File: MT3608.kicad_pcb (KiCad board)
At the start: 2 copper layers, 40 x 20 mm, 19 parts, among them J1 IN, J2 OUT, U1 MT3608

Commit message: Take 2
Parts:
- removed D1: SBR3U, Diode_SMD:D_PowerDI-123
- D2: value 1N4148 -> MBR0540; footprint Diode_THT:D_DO-35_SOD27_P7.62mm_Horizontal -> Diode_SMD:D_SOD-123
- moved TP6 13.7 mm to (102.8, 103.7)
- moved D2 12.5 mm to (113.1, 115.3), turned to 0 degrees
- moved TP2 11.4 mm to (107.9, 108.7)
- moved TP1 7.62 mm to (107.9, 103.7)
- moved R2 6.70 mm to (107.6, 118.0), turned to 180 degrees
- moved C4 5.50 mm to (107.7, 114.5), turned to 180 degrees
- moved R6 5.34 mm to (107.7, 112.0)
- moved J2 5.08 mm to (102.8, 108.7)
- moved TP7 5.08 mm to (102.8, 116.3)
- moved R1 1.16 mm to (112.8, 118.1), turned to 180 degrees
- moved L1 0.39 mm to (117.9, 106.6)
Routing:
- net Net-(D2-K): track 38.5 -> 12.9 mm, vias 1 -> 0
- net Net-(D2-A): track 30.2 -> 20.2 mm
- net Net-(U1-FB): track 11.4 -> 21.4 mm, vias 0 -> 2
- net Net-(J2-Pin_1): track 10.8 -> 5.25 mm
- net GND: track 0.00 -> 5.01 mm
- net Net-(U1-EN): track 23.1 -> 25.3 mm
- added copper zone on B.Cu, net GND
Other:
- board size 40 x 20 mm -> 35 x 22 mm

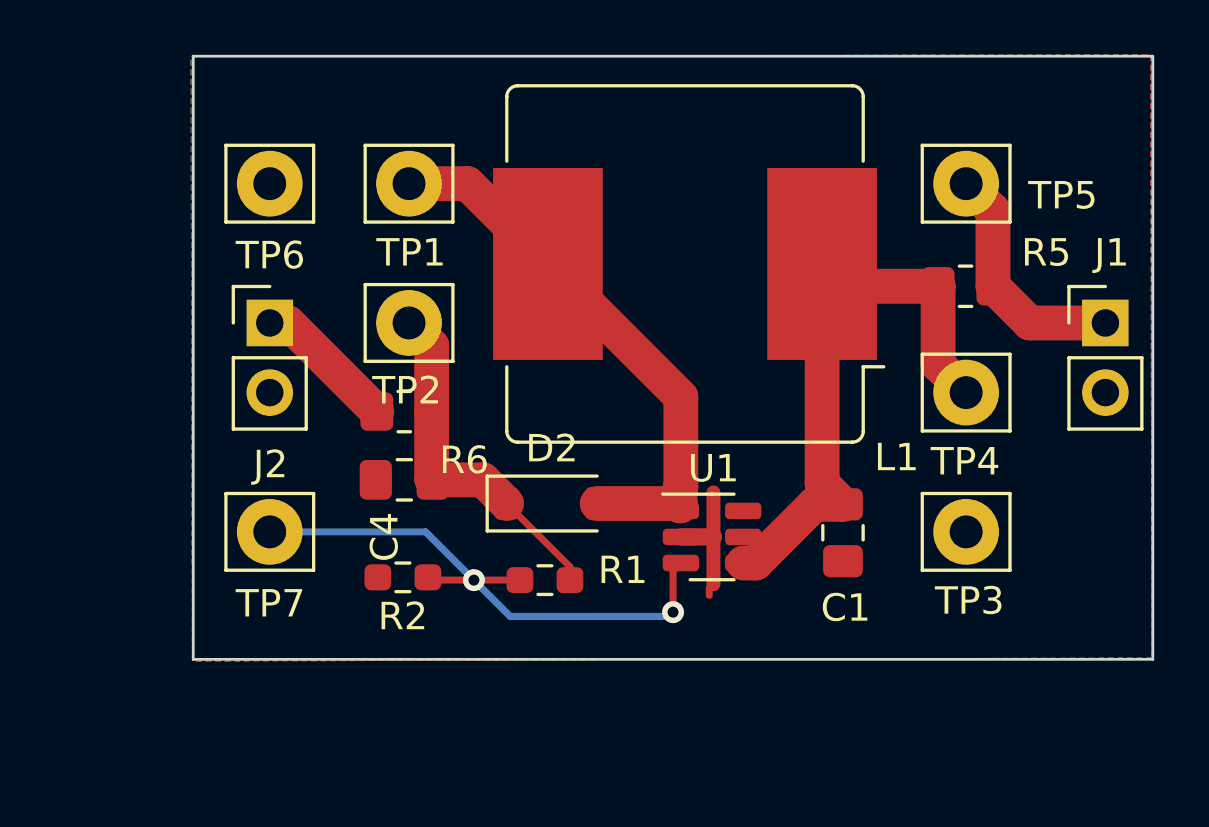
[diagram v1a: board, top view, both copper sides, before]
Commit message: 27V works; corrected TP6
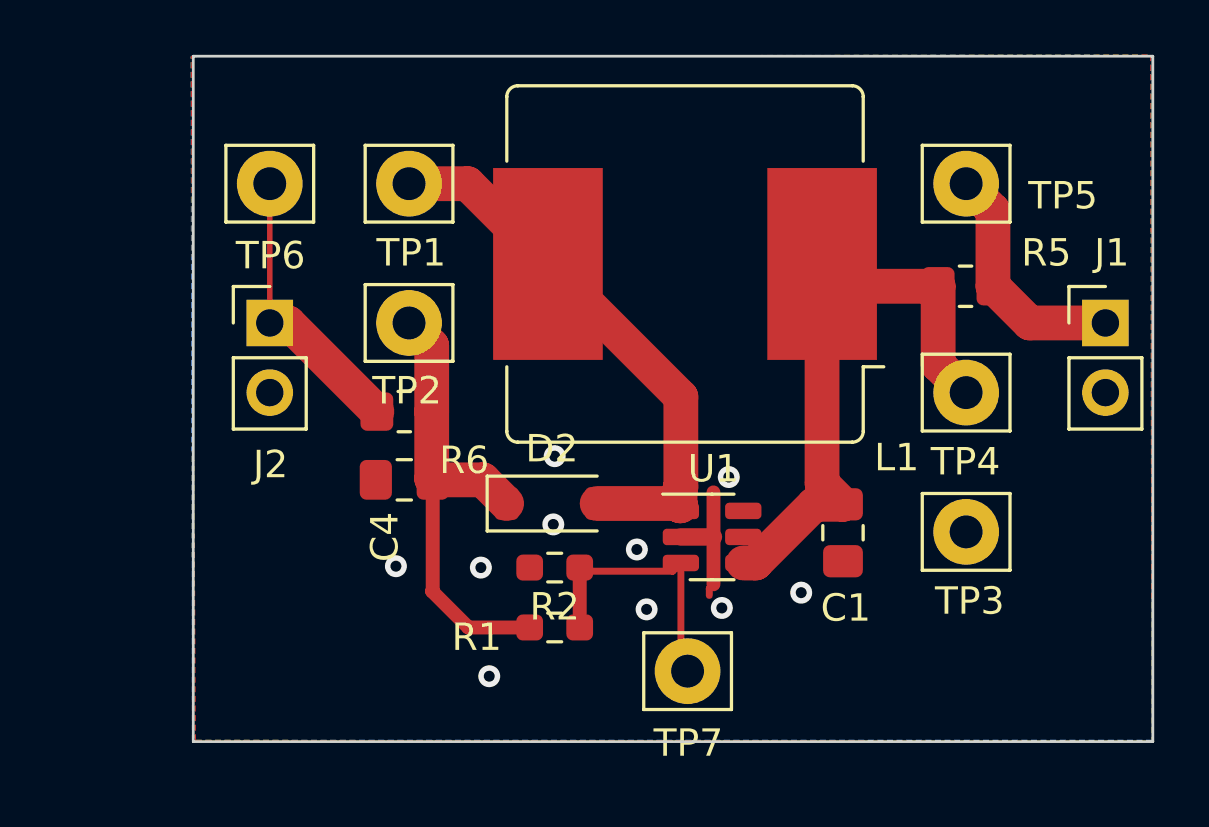
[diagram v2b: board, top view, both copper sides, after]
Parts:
- moved TP7 16.1 mm to (118.0, 121.4)
- moved R2 5.55 mm to (113.2, 117.7)
- moved R1 1.76 mm to (113.2, 119.8), turned to 0 degrees
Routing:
- net Net-(U1-FB): track 21.4 -> 10.1 mm, vias 2 -> 0
- net Net-(D2-K): track 12.9 -> 17.3 mm
- net GND: vias 0 -> 10
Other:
- board size 35 x 22 mm -> 35 x 25 mm
